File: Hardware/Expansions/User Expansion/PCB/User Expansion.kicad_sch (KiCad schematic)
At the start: 35 parts, among them J101 10018784-10201TLF, U101 M24C02-FMN

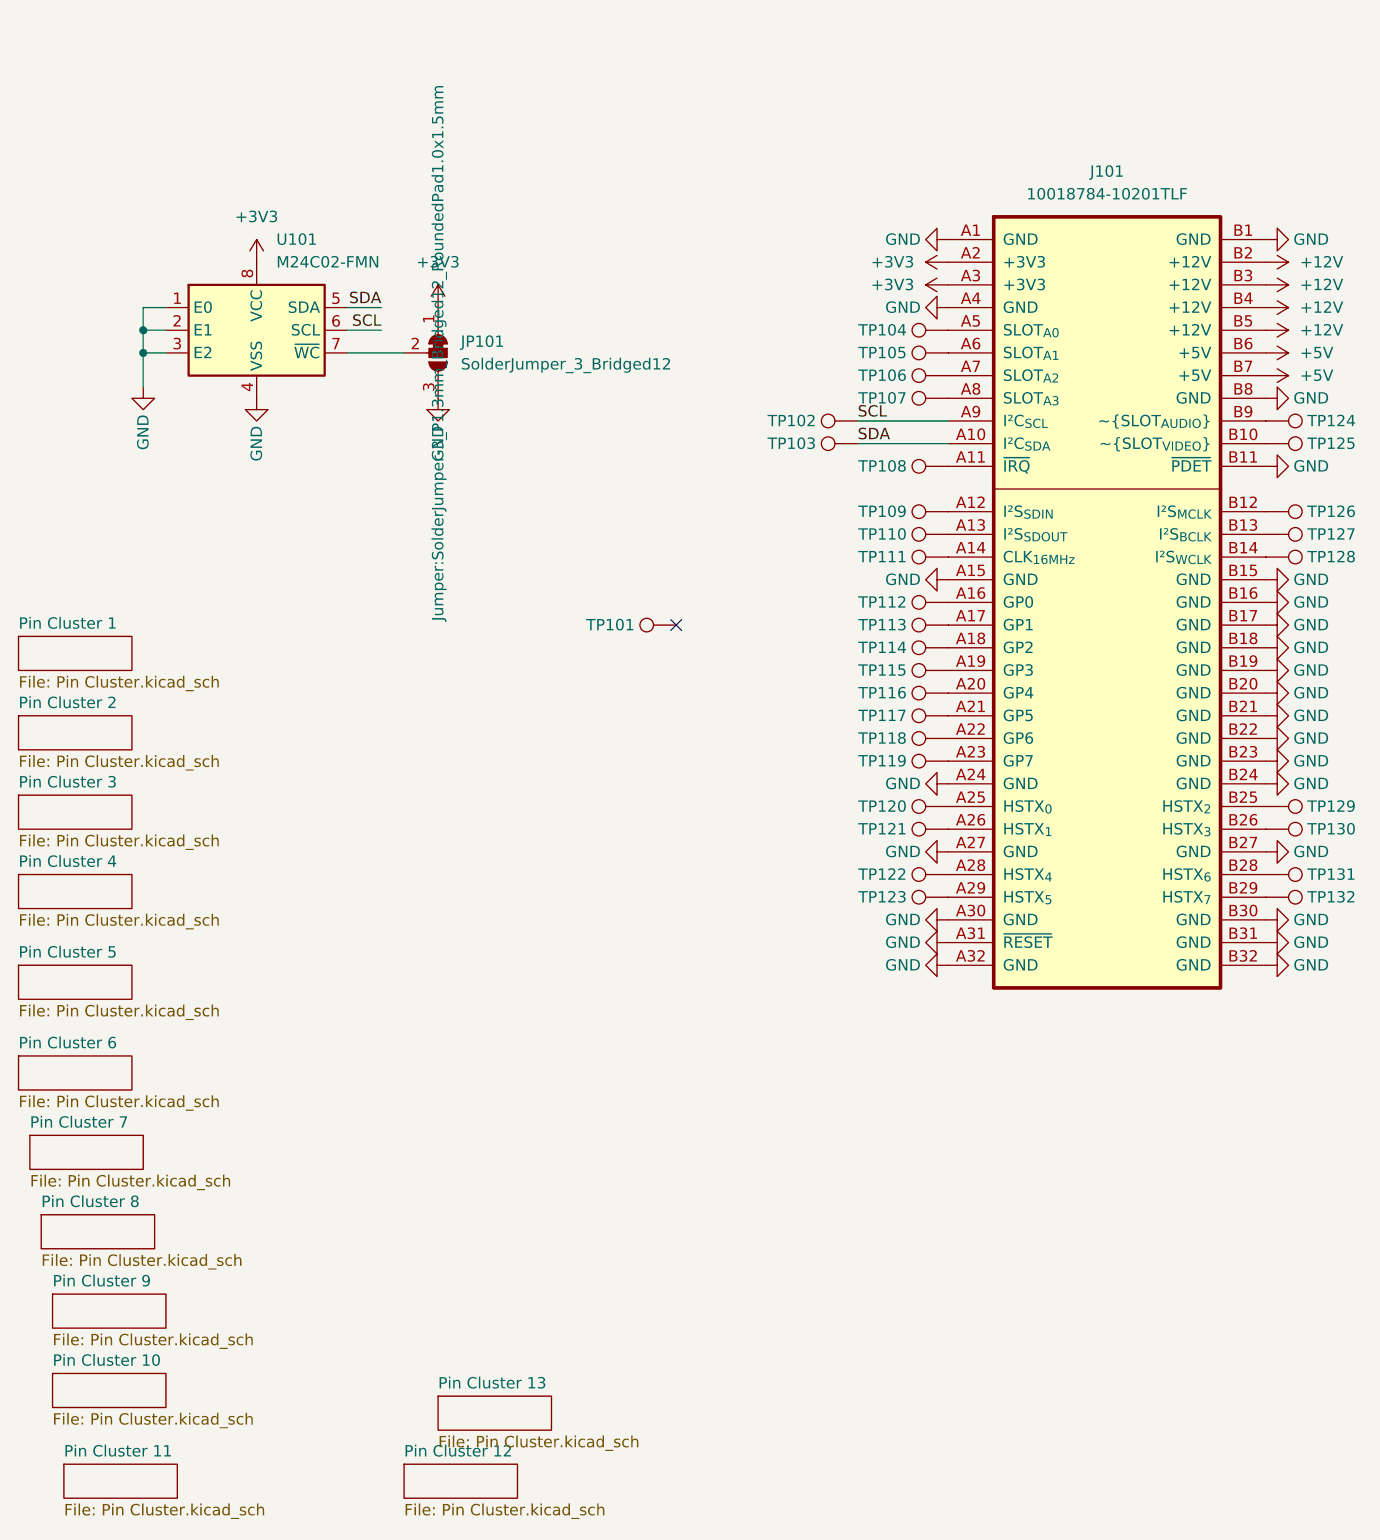
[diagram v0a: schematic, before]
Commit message: Continues work on User Expansion design, adds CI for exports, ERC and DRC
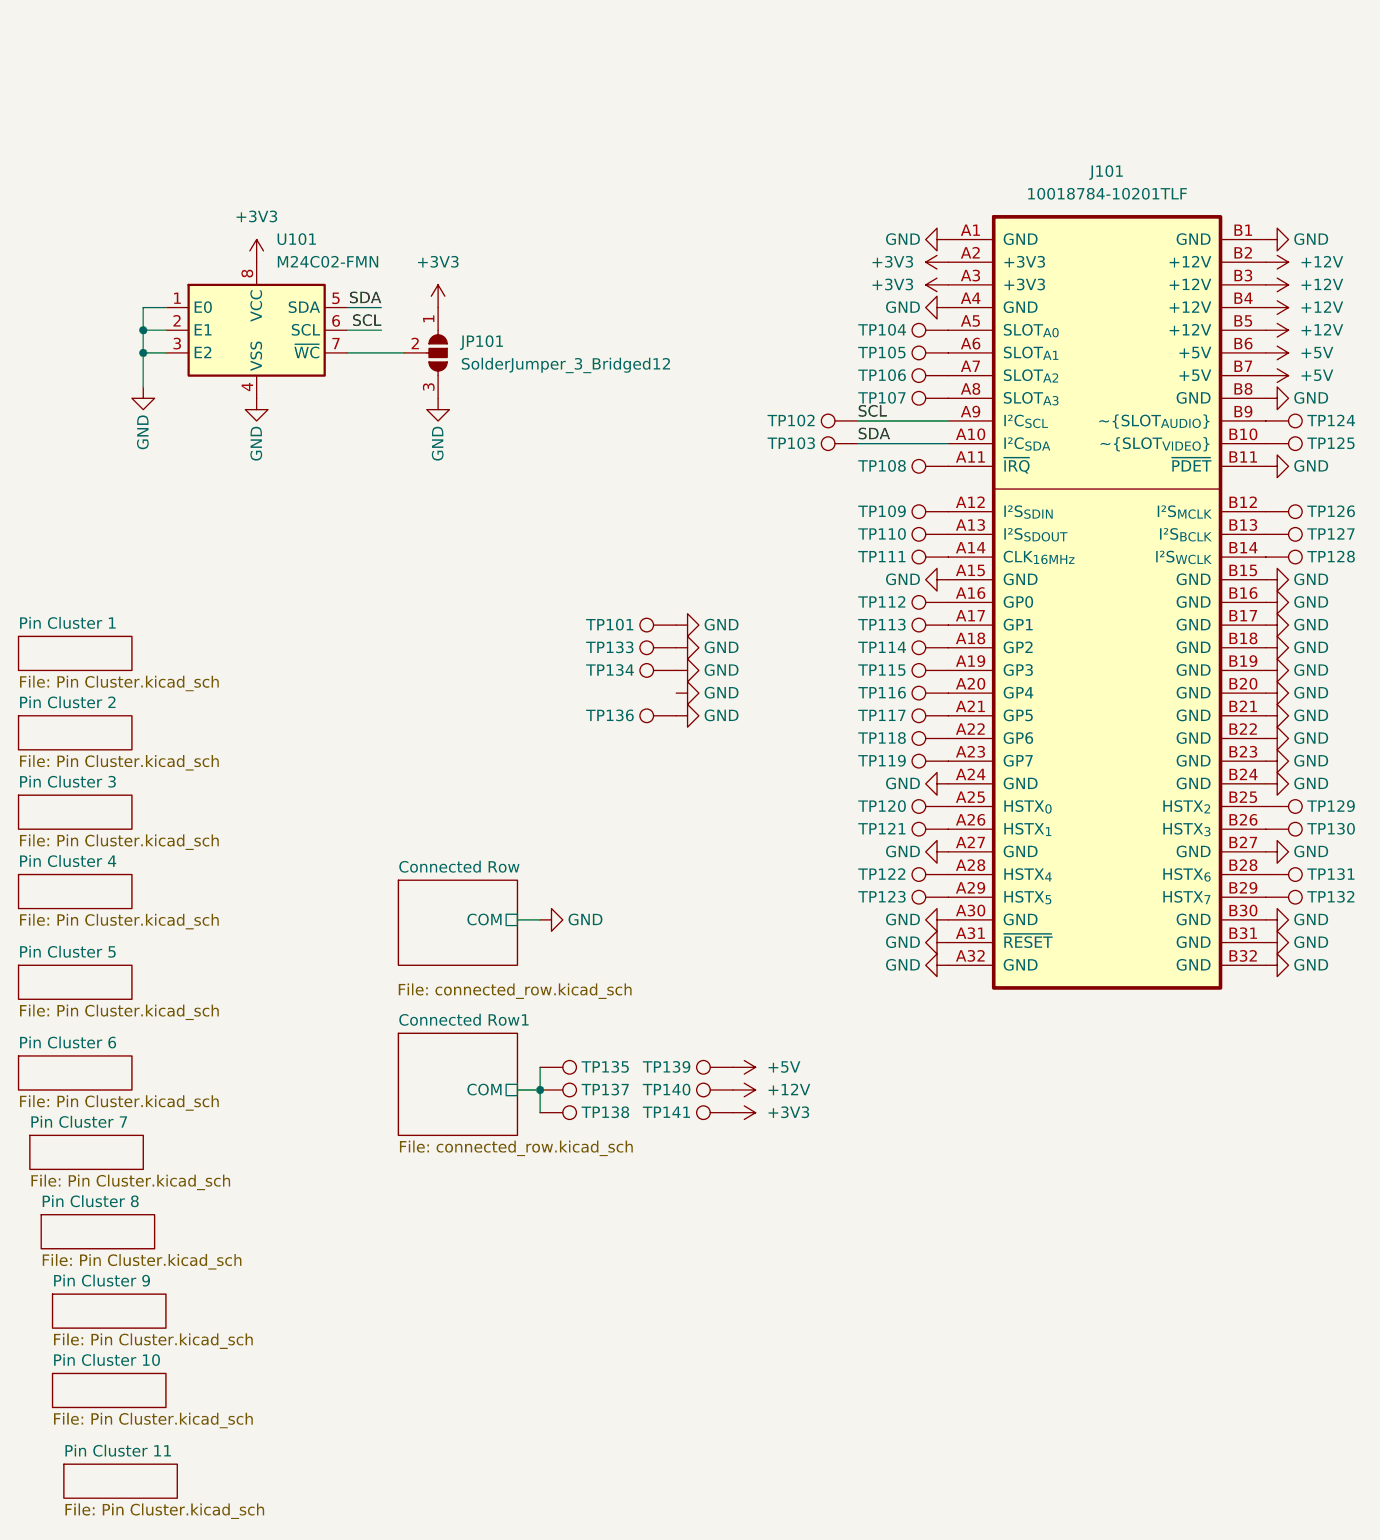
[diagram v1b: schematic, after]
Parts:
- added TP133, TP134, TP135, TP136, TP137, TP138, TP139, TP140, TP141: GP7, TestPoint:TestPoint_THTPad_D1.5mm_Drill0.7mm, symbol Connector:TestPoint
- JP101: footprint Jumper:SolderJumper-3_P1.3mm_Bridged12_RoundedPad1.0x1.5mm -> Jumper:SolderJumper-3_P1.3mm_Open_RoundedPad1.0x1.5mm; symbol Jumper:SolderJumper_3_Bridged12 -> Jumper:SolderJumper_3_Open
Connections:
- net +12V: now also TP140.1
- net +3V3: now also TP141.1
- net +5V: now also TP139.1
- net GND: now also TP101.1, TP133.1, TP134.1, TP136.1
- new net Connected Row1/COM: TP135.1, TP137.1, TP138.1
- no-connect marks 1 -> 0
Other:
- removed sheet Pin Cluster 12
- removed sheet Pin Cluster 13
- added sheet Connected Row (connected_row.kicad_sch)
- added sheet Connected Row1 (connected_row.kicad_sch)
- company: (none) -> Ashet Technologies
- title: (none) -> User Expansion
